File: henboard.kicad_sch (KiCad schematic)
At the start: 23 parts, among them J4 5077CR-16SMC2-BK-TR, Q1 UMH3N, U1 LDL1117S33R, U2 ESP32-S3-WROOM-1, U3 CP2102N-Axx-xQFN28, U4 USBLC6-2P6

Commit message: Assign footprints to henboard
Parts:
- J4: footprint 5077CR-16SMC2-BK-TR:NELTRON_5077CR-16SMC2-BK-TR -> 5077CR-16SMC2-BK-TR:5077CR-16SMC2-BK-TR
- S1, S2: footprint SKRPACE010:SW_SKRPACE010 -> SKRPACE010:SKRPACE010
- U1: footprint LDL1117S33R:SOT230P700X180-4N -> LDL1117S33R:LDL1117S33R
- U2: footprint (none) -> RF_Module:ESP32-S3-WROOM-1
- U3: footprint (none) -> Package_DFN_QFN:QFN-28-1EP_5x5mm_P0.5mm_EP3.35x3.35mm
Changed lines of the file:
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@@
 			)
 		)
-		(property "Footprint" ""
+		(property "Footprint" "RF_Module:ESP32-S3-WROOM-1"
 			(at 251.46 101.6 0)
 			(effects
@@
 			)
 		)
-		(property "Footprint" "5077CR-16SMC2-BK-TR:NELTRON_5077CR-16SMC2-BK-TR"
+		(property "Footprint" "5077CR-16SMC2-BK-TR:5077CR-16SMC2-BK-TR"
 			(at 36.83 125.73 0)
 			(effects
@@
 			)
 		)
-		(property "Footprint" "SKRPACE010:SW_SKRPACE010"
+		(property "Footprint" "SKRPACE010:SKRPACE010"
 			(at 34.29 41.91 0)
 			(effects
@@
 			)
 		)
-		(property "Footprint" "LDL1117S33R:SOT230P700X180-4N"
+		(property "Footprint" "LDL1117S33R:LDL1117S33R"
 			(at 109.22 33.02 0)
 			(effects
@@
 			)
 		)
-		(property "Footprint" "SKRPACE010:SW_SKRPACE010"
+		(property "Footprint" "SKRPACE010:SKRPACE010"
 			(at 64.77 41.91 0)
 			(effects
@@
 			)
 		)
-		(property "Footprint" ""
+		(property "Footprint" "Package_DFN_QFN:QFN-28-1EP_5x5mm_P0.5mm_EP3.35x3.35mm"
 			(at 152.4 116.84 0)
 			(effects

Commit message: Change schematic
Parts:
- added J1, J10, J11, J12, J13, J14, J15, J16, J17, J18, J19, J2, J20, J21, J3, J5, J6, J7, J8, J9: Conn_01x01, Pad-CapacitiveTouch:Pad-CapacitiveTouch, symbol Connector_Generic:Conn_01x01
- added S3, S4, S5, S6: SKRPACE010, SKRPACE010:SKRPACE010, symbol SKRPACE010:SKRPACE010
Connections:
- net TOUCH1: now also J1.1 (Pin_1)
- net TOUCH10: now also J11.1 (Pin_1)
- net TOUCH11: now also J12.1 (Pin_1), J21.1 (Pin_1)
- net TOUCH12: now also J13.1 (Pin_1)
- net TOUCH13: now also J15.1 (Pin_1), J17.1 (Pin_1), J19.1 (Pin_1)
- net TOUCH14: now also J14.1 (Pin_1), J16.1 (Pin_1), J18.1 (Pin_1)
- net TOUCH2: now also J2.1 (Pin_1)
- net TOUCH3: now also J3.1 (Pin_1)
- net TOUCH4: now also J5.1 (Pin_1)
- net TOUCH5: now also J6.1 (Pin_1)
- net TOUCH6: now also J7.1 (Pin_1)
- net TOUCH7: now also J8.1 (Pin_1)
- net TOUCH8: now also J9.1 (Pin_1)
- net TOUCH9: now also J10.1 (Pin_1), J20.1 (Pin_1)
- net SELECT3: now reaches U2.10 (GPIO17/U1TXD/ADC2_CH6)
- net SELECT3: now also S5.1
- net SELECT4: now reaches U2.11 (GPIO18/U1RXD/ADC2_CH7/CLK_OUT3)
- net SELECT4: now also S6.1
- net SELECT1: now reaches U2.8 (GPIO15/U0RTS/ADC2_CH4/XTAL_32K_P)
- net SELECT1: now also S3.1
- net SELECT2: now reaches U2.9 (GPIO16/U0CTS/ADC2_CH5/XTAL_32K_N)
- net SELECT2: now also S4.1
- net Earth renamed GND
- net GND: now also S3.4, S4.4, S5.4, S6.4
- no-connect marks 41 -> 45

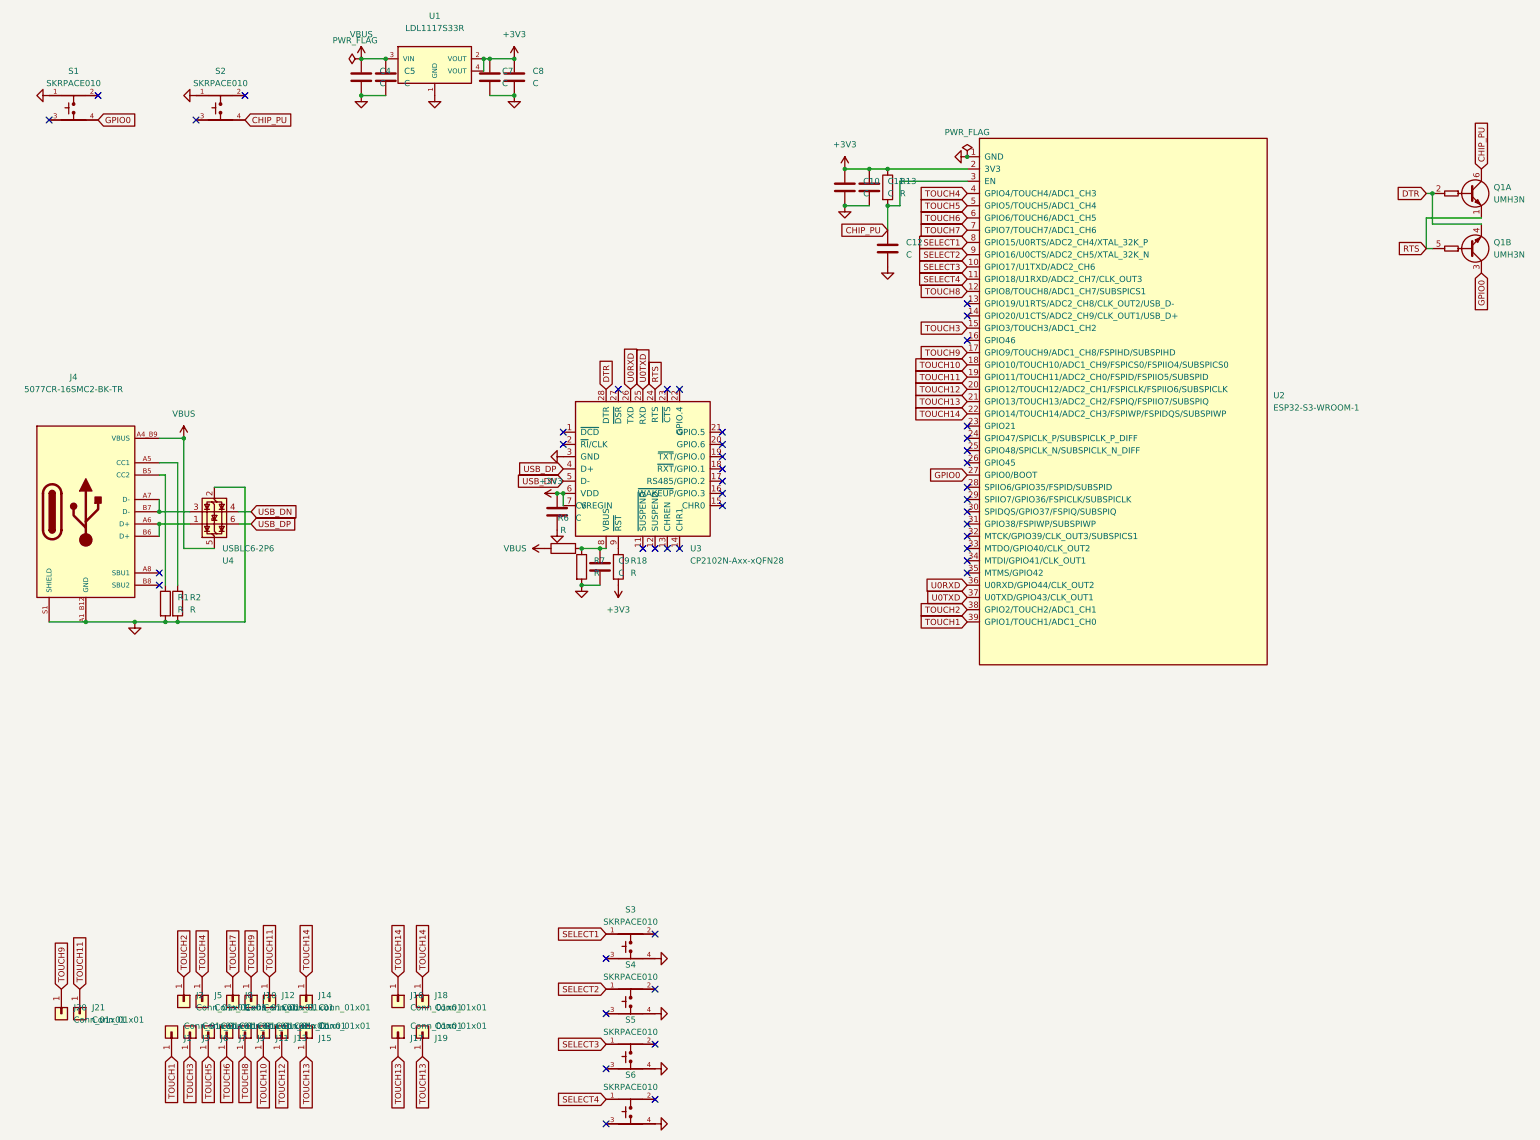
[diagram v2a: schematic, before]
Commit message: Change schematic annotation and footprint assignments
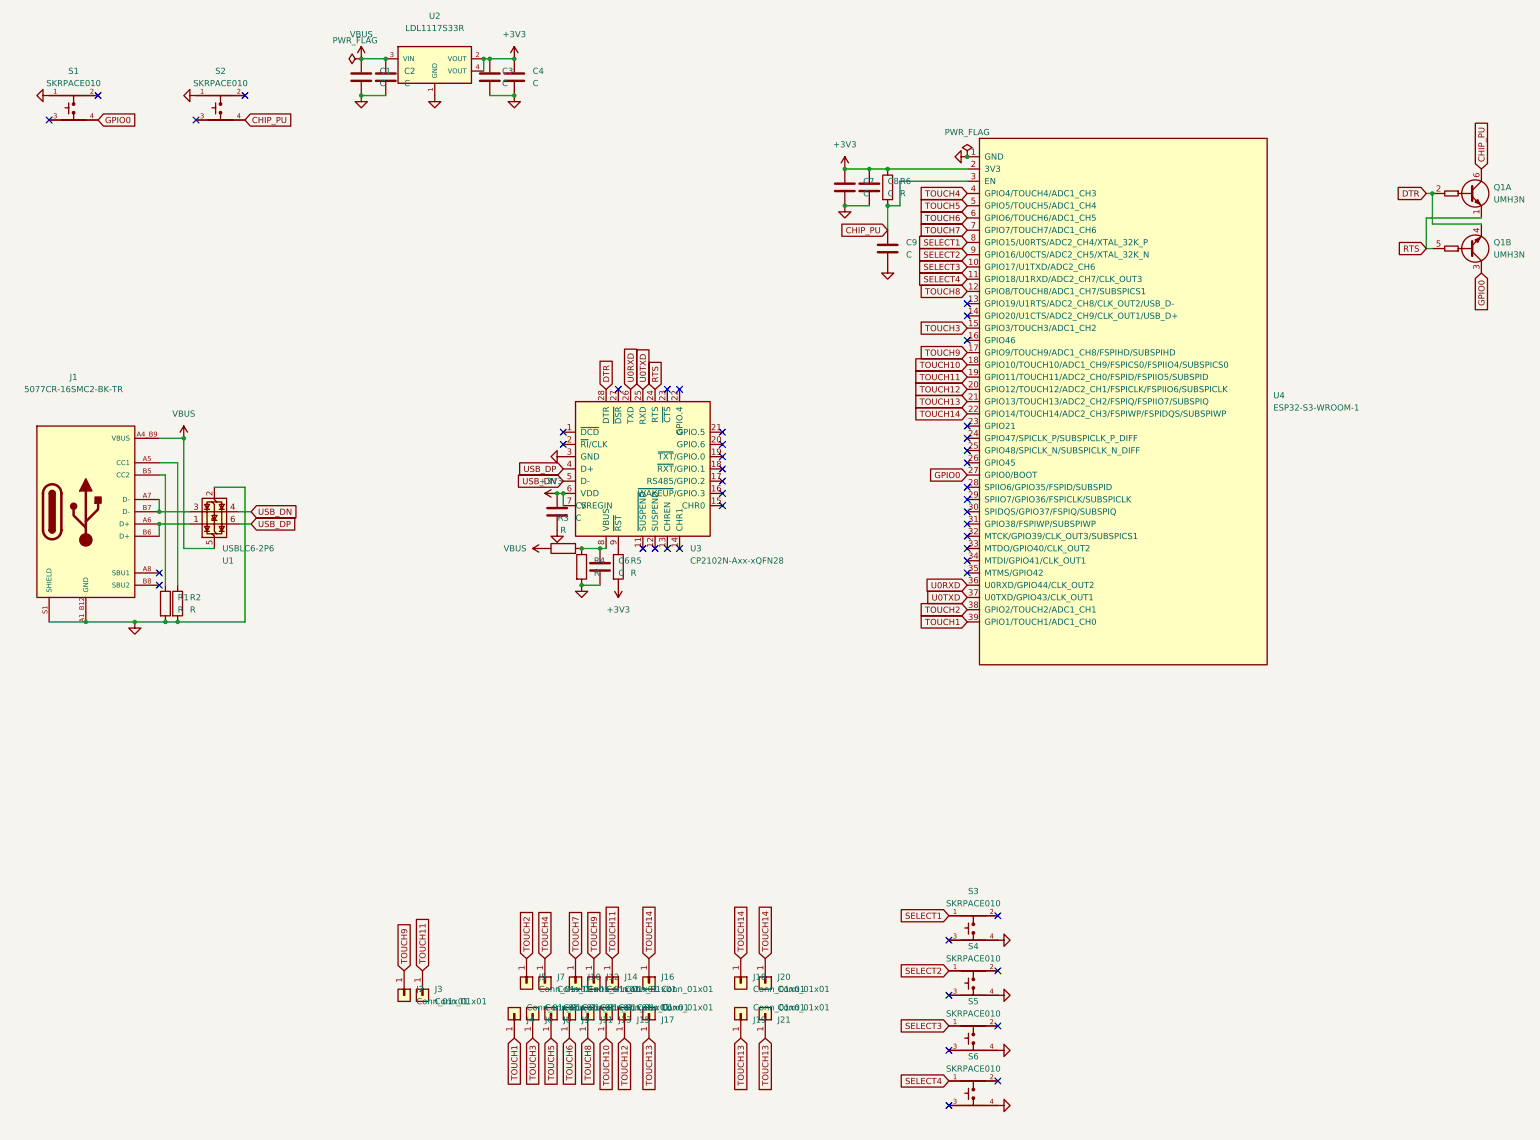
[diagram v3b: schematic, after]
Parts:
- J10: renamed from J8; footprint Pad-CapacitiveTouch:Pad-CapacitiveTouch -> Pad-CapacitiveTouch:Pad-CapacitiveTouch-small
- J11: renamed from J9; footprint Pad-CapacitiveTouch:Pad-CapacitiveTouch -> Pad-CapacitiveTouch:Pad-CapacitiveTouch-small
- J12: renamed from J10; footprint Pad-CapacitiveTouch:Pad-CapacitiveTouch -> Pad-CapacitiveTouch:Pad-CapacitiveTouch-small
- J13: renamed from J11; footprint Pad-CapacitiveTouch:Pad-CapacitiveTouch -> Pad-CapacitiveTouch:Pad-CapacitiveTouch-small
- J14: renamed from J12; footprint Pad-CapacitiveTouch:Pad-CapacitiveTouch -> Pad-CapacitiveTouch:Pad-CapacitiveTouch-small
- J15: renamed from J13; footprint Pad-CapacitiveTouch:Pad-CapacitiveTouch -> Pad-CapacitiveTouch:Pad-CapacitiveTouch-small
- J16: renamed from J14; footprint Pad-CapacitiveTouch:Pad-CapacitiveTouch -> Pad-CapacitiveTouch:Pad-CapacitiveTouch-small
- J17: renamed from J15; footprint Pad-CapacitiveTouch:Pad-CapacitiveTouch -> Pad-CapacitiveTouch:Pad-CapacitiveTouch-small
- J18: renamed from J16; footprint Pad-CapacitiveTouch:Pad-CapacitiveTouch -> Pad-CapacitiveTouch:Pad-CapacitiveTouch-small
- J19: renamed from J17; footprint Pad-CapacitiveTouch:Pad-CapacitiveTouch -> Pad-CapacitiveTouch:Pad-CapacitiveTouch-small
- J2: renamed from J20; footprint Pad-CapacitiveTouch:Pad-CapacitiveTouch -> Pad-CapacitiveTouch:Pad-CapacitiveTouch-small
- J20: renamed from J18; footprint Pad-CapacitiveTouch:Pad-CapacitiveTouch -> Pad-CapacitiveTouch:Pad-CapacitiveTouch-small
- J21: renamed from J19; footprint Pad-CapacitiveTouch:Pad-CapacitiveTouch -> Pad-CapacitiveTouch:Pad-CapacitiveTouch-small
- J3: renamed from J21; footprint Pad-CapacitiveTouch:Pad-CapacitiveTouch -> Pad-CapacitiveTouch:Pad-CapacitiveTouch-small
- J4: renamed from J1; footprint Pad-CapacitiveTouch:Pad-CapacitiveTouch -> Pad-CapacitiveTouch:Pad-CapacitiveTouch-small
- J5: renamed from J2; footprint Pad-CapacitiveTouch:Pad-CapacitiveTouch -> Pad-CapacitiveTouch:Pad-CapacitiveTouch-small
- J6: renamed from J3; footprint Pad-CapacitiveTouch:Pad-CapacitiveTouch -> Pad-CapacitiveTouch:Pad-CapacitiveTouch-small
- J7: renamed from J5; footprint Pad-CapacitiveTouch:Pad-CapacitiveTouch -> Pad-CapacitiveTouch:Pad-CapacitiveTouch-small
- J8: renamed from J6; footprint Pad-CapacitiveTouch:Pad-CapacitiveTouch -> Pad-CapacitiveTouch:Pad-CapacitiveTouch-small
- J9: renamed from J7; footprint Pad-CapacitiveTouch:Pad-CapacitiveTouch -> Pad-CapacitiveTouch:Pad-CapacitiveTouch-small
- renumbered C4 to C1, C5 to C2, C7 to C3, C8 to C4, C6 to C5, C9 to C6, C10 to C7, C11 to C8, C12 to C9, J4 to J1, R6 to R3, R7 to R4, R18 to R5, R13 to R6, U4 to U1, U1 to U2, U2 to U4
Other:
- moved on the sheet: J10, J11, J12, J13, J14, J15, J16, J17, J18, J19, J2, J20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

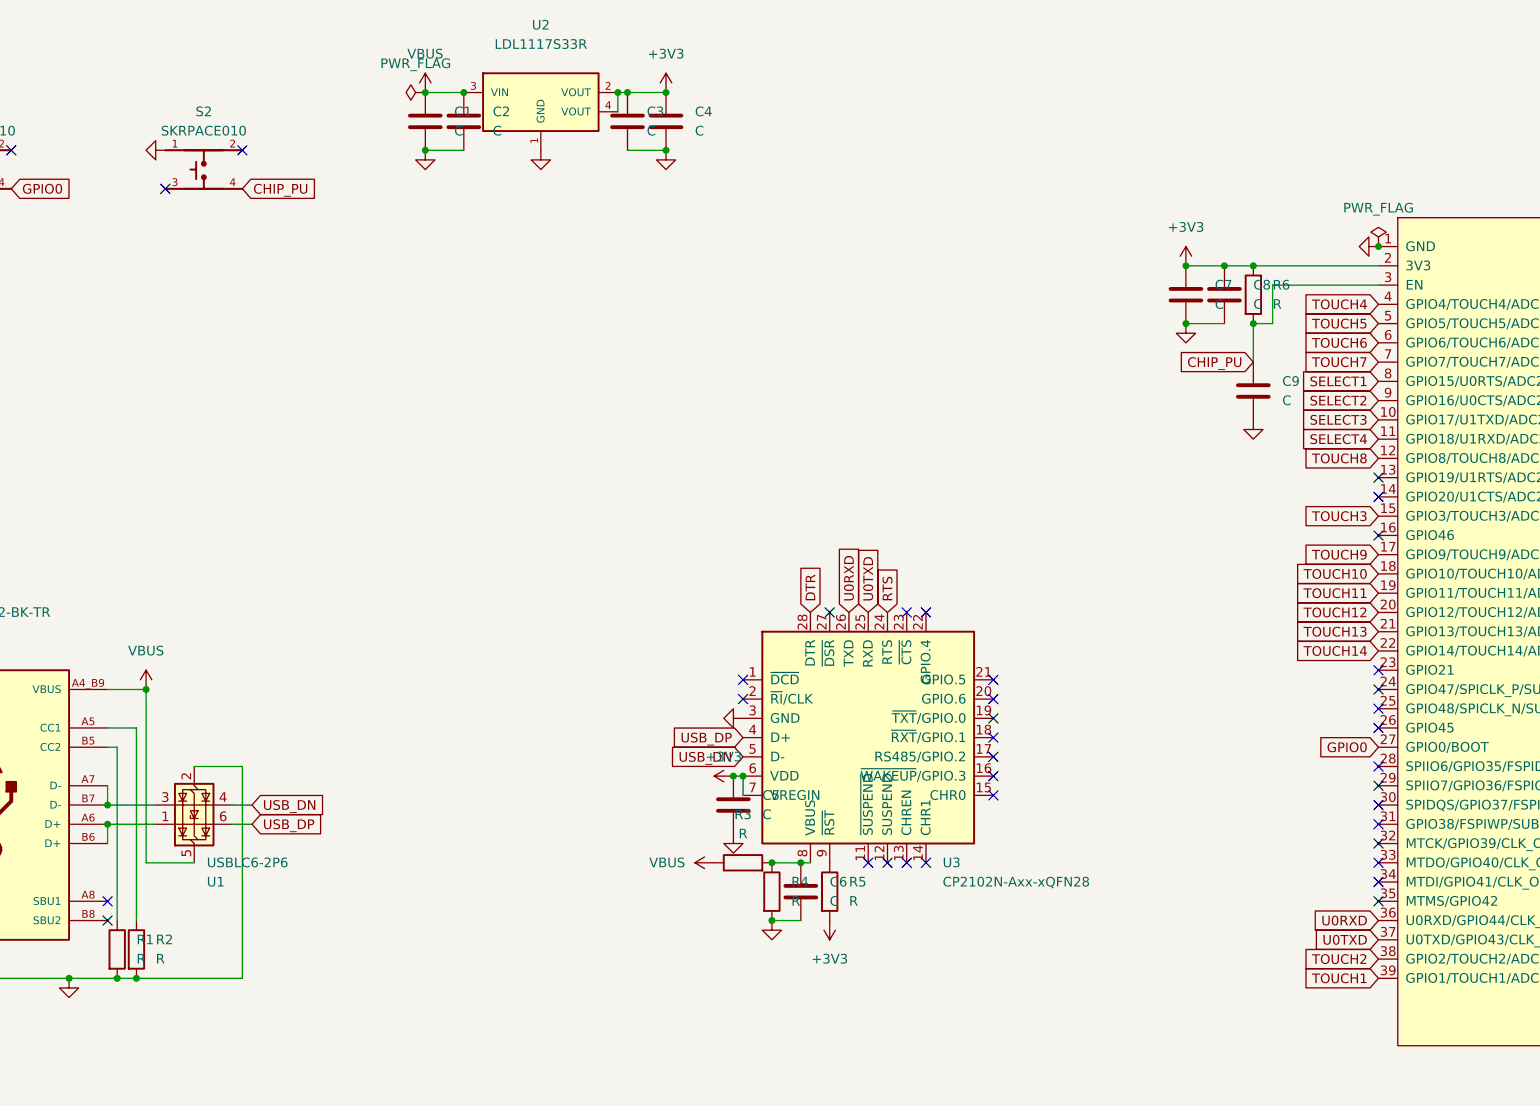
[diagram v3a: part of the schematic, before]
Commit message: Add specific values to schematic
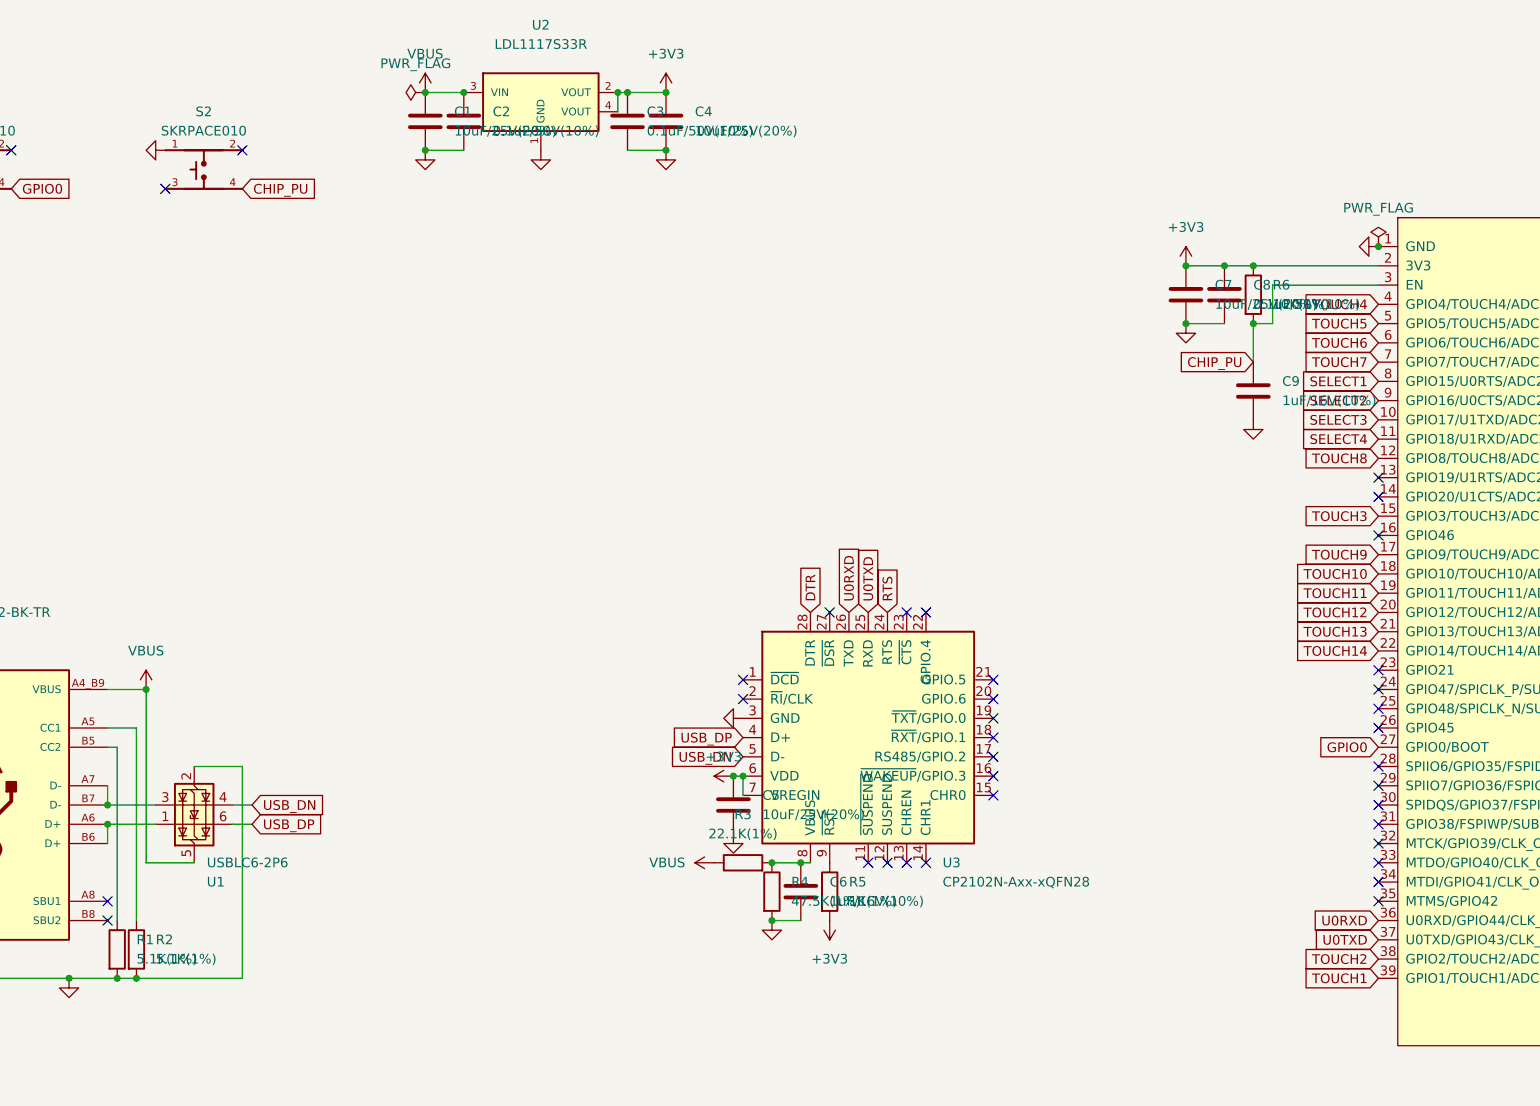
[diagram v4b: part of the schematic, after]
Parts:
- C1, C4, C5, C7: value C -> 10uF/25V(20%)
- C2, C3, C8: value C -> 0.1uF/50V(10%)
- C6, C9: value C -> 1uF/16V(10%)
- R1, R2: value R -> 5.1K(1%)
- R3: value R -> 22.1K(1%)
- R4: value R -> 47.5K(1%)
- R5: value R -> 1K(1%)
- R6: value R -> 10K(1%)
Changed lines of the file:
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@@
 			)
 		)
-		(property "Value" "R"
+		(property "Value" "47.5K(1%)"
 			(at 142.24 138.4299 0)
 			(effects
@@
 			)
 		)
-		(property "Value" "C"
+		(property "Value" "10uF/25V(20%)"
 			(at 138.43 126.9999 0)
 			(effects
@@
 			)
 		)
-		(property "Value" "C"
+		(property "Value" "0.1uF/50V(10%)"
 			(at 203.2 59.6899 0)
 			(effects
@@
 			)
 		)
-		(property "Value" "C"
+		(property "Value" "0.1uF/50V(10%)"
 			(at 123.19 36.8299 0)
 			(effects
@@
 			)
 		)
-		(property "Value" "C"
+		(property "Value" "1uF/16V(10%)"
 			(at 207.01 72.3899 0)
 			(effects
@@
 			)
 		)
-		(property "Value" "C"
+		(property "Value" "10uF/25V(20%)"
 			(at 198.12 59.6899 0)
 			(effects
@@
 			)
 		)
-		(property "Value" "C"
+		(property "Value" "1uF/16V(10%)"
 			(at 147.32 138.4299 0)
 			(effects
@@
 			)
 		)
-		(property "Value" "R"
+		(property "Value" "22.1K(1%)"
 			(at 135.89 129.54 90)
 			(effects
@@
 			)
 		)
-		(property "Value" "C"
+		(property "Value" "10uF/25V(20%)"
 			(at 97.79 36.8299 0)
 			(effects
@@
 			)
 		)
-		(property "Value" "R"
+		(property "Value" "5.1K(1%)"
 			(at 55.88 146.0499 0)
 			(effects
@@
 			)
 		)
-		(property "Value" "C"
+		(property "Value" "10uF/25V(20%)"
 			(at 129.54 36.8299 0)
 			(effects
@@
 			)
 		)
-		(property "Value" "R"
+		(property "Value" "10K(1%)"
 			(at 205.74 59.6899 0)
 			(effects
@@
 			)
 		)
-		(property "Value" "R"
+		(property "Value" "1K(1%)"
 			(at 149.86 138.4299 0)
 			(effects
@@
 			)
 		)
-		(property "Value" "R"
+		(property "Value" "5.1K(1%)"
 			(at 58.42 146.0499 0)
 			(effects
@@
 			)
 		)
-		(property "Value" "C"
+		(property "Value" "0.1uF/50V(10%)"
 			(at 102.87 36.8299 0)
 			(effects
